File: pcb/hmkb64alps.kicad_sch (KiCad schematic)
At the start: 21 parts, among them J1 AVR-ISP-6, SW69 SW_Push, U1 ATmega32U4-A, Y1 16MHz

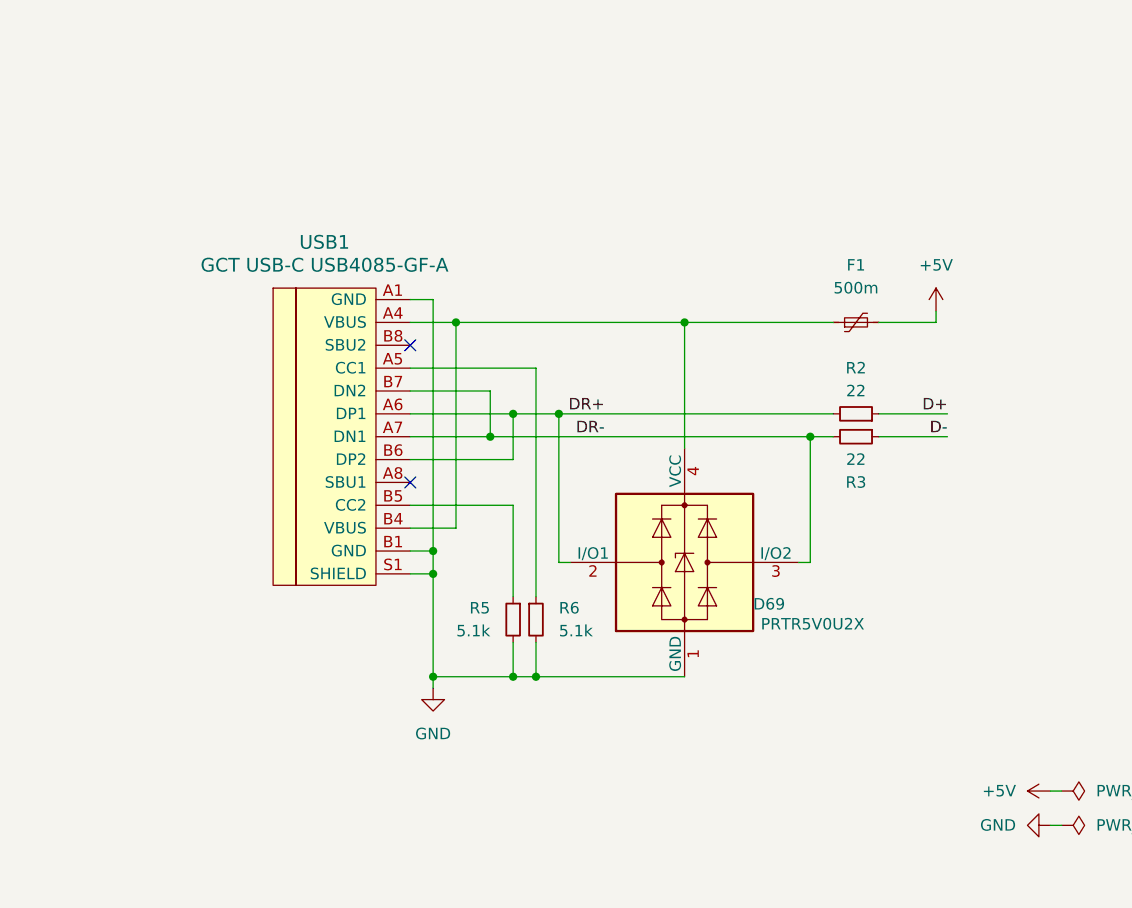
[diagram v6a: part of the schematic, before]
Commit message: add and switch to yet a different usb-c connector
also prepare a nicer symbol and clean up libraries
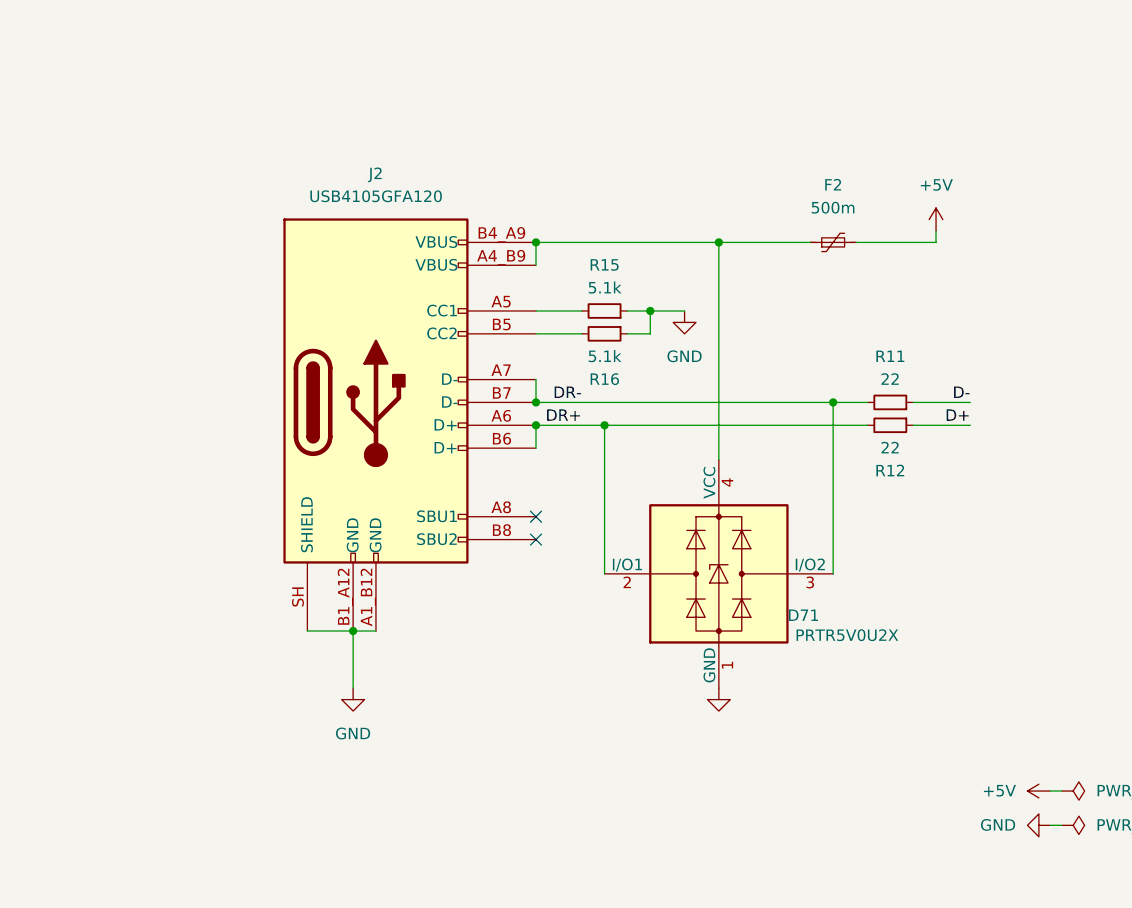
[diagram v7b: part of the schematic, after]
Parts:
- removed D69: PRTR5V0U2X, Package_TO_SOT_SMD:SOT-143, symbol Power_Protection:PRTR5V0U2X
- removed F1: 500m, Fuse:Fuse_1206_3216Metric_Pad1.42x1.75mm_HandSolder, symbol Device:Polyfuse_Small
- removed R2, R3: 22, Resistor_SMD:R_0805_2012Metric_Pad1.20x1.40mm_HandSolder, symbol Device:R_Small
- removed R5, R6: 5.1k, Resistor_SMD:R_0805_2012Metric_Pad1.20x1.40mm_HandSolder, symbol Device:R_Small
- removed USB1: GCT USB-C USB4085-GF-A, Connector_USB:USB_C_Receptacle_HRO_TYPE-C-31-M-12, symbol hmkb64alps:GCT USB-C USB4085-GF-A
- added D71: PRTR5V0U2X, Package_TO_SOT_SMD:SOT-143, symbol Power_Protection:PRTR5V0U2X
- added F2: 500m, Fuse:Fuse_1206_3216Metric_Pad1.42x1.75mm_HandSolder, symbol Device:Polyfuse_Small
- added J2: USB4105GFA120, kbd_custom:GCT_USB4105GFA120, symbol kbd_custom:USB_C_Receptacle_USB2.0_16P
- added R11, R12: 22, Resistor_SMD:R_0805_2012Metric_Pad1.20x1.40mm_HandSolder, symbol Device:R_Small
- added R15, R16: 5.1k, Resistor_SMD:R_0805_2012Metric_Pad1.20x1.40mm_HandSolder, symbol Device:R_Small
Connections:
- net +5V: now also F2.2
- net D+: now also R12.1
- net D-: now also R11.1
- net DR+: now also D71.2 (I/O1), J2.A6 (D+), J2.B6 (D+), R12.2
- net DR-: now also D71.3 (I/O2), J2.A7 (D-), J2.B7 (D-), R11.2
- net GND: now also D71.1 (GND), J2.A1_B12 (GND), J2.B1_A12 (GND), J2.SH (SHIELD), R15.1, R16.1
- new net: D71.4 (VCC), F2.1, J2.A4_B9 (VBUS), J2.B4_A9 (VBUS)
- new net: J2.B5 (CC2), R16.2
- new net: J2.A5 (CC1), R15.2
